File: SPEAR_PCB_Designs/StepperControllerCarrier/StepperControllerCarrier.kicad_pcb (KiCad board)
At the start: 2 copper layers, 108 x 49 mm, 19 parts, among them J1 Conn_01x02_Pin, J2 Conn_01x02_Pin, J3 Conn_01x02_Pin, J4 Conn_01x02_Pin, J5 Conn_01x04_Pin, U1 AP63203WU

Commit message: Fixed this finally
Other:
- board text removed: "2973"
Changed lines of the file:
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@@
 			(drillshape 0)
 			(scaleselection 1)
-			(outputdirectory "Fabrication")
+			(outputdirectory "C:/Users/Ammar/Spear/Stepper_Motor_Controller_Carrier_Board/Fabrication/")
 		)
 	)
@@
 		)
 		(property "Value" "Motor_Driver_Board_2973"
-			(at 12.7 19.82 0)
+			(at 12.7 17.8 0)
 			(unlocked yes)
 			(layer "F.Fab")
@@
 			)
 		)
-		(model "${SPEAR_PCB_2026_DIR}/SPEAR_3D_Models/SPEAR_MotorControllerCarrier/tb67s2x9ftg-stepper-motor-driver-carrier.step"
-			(offset
-				(xyz 0 -35.5 8.5)
-			)
-			(scale
-				(xyz 1 1 1)
-			)
-			(rotate
-				(xyz -0 -0 -0)
-			)
-		)
 	)
 	(footprint "SPEAR_Connectors:JST_XH_S4B-XH-A-1_1x04_P2.50mm_Horizontal"
@@
 		)
 	)
-	(gr_text "2973"
-		(at 167 99 0)
-		(layer "F.SilkS")
-		(effects
-			(font
-				(size 1 1)
-				(thickness 0.15)
-			)
-		)
-	)
 	(gr_text "MOTOR B"
 		(at 184.25 108.5 270)
@@
 	)
 	(segment
-		(start 152.2 112.55)
-		(end 152.2 110.26)
+		(start 152 112.75)
+		(end 152 110.46)
 		(width 0.3)
 		(layer "F.Cu")
@@
 	)
 	(segment
-		(start 138.98 114.1)
-		(end 139.175 114.295)
+		(start 139.175 114.295)
+		(end 150.455 114.295)
 		(width 0.3)
 		(layer "F.Cu")
@@
 	)
 	(segment
-		(start 150.455 114.295)
-		(end 152.2 112.55)
+		(start 152 110.46)
+		(end 154.57 107.89)
 		(width 0.3)
 		(layer "F.Cu")
@@
 	)
 	(segment
-		(start 152.2 110.26)
-		(end 154.57 107.89)
+		(start 150.455 114.295)
+		(end 152 112.75)
 		(width 0.3)
 		(layer "F.Cu")
@@
 	)
 	(segment
-		(start 139.175 114.295)
-		(end 150.455 114.295)
+		(start 138.98 114.1)
+		(end 139.175 114.295)
 		(width 0.3)
 		(layer "F.Cu")

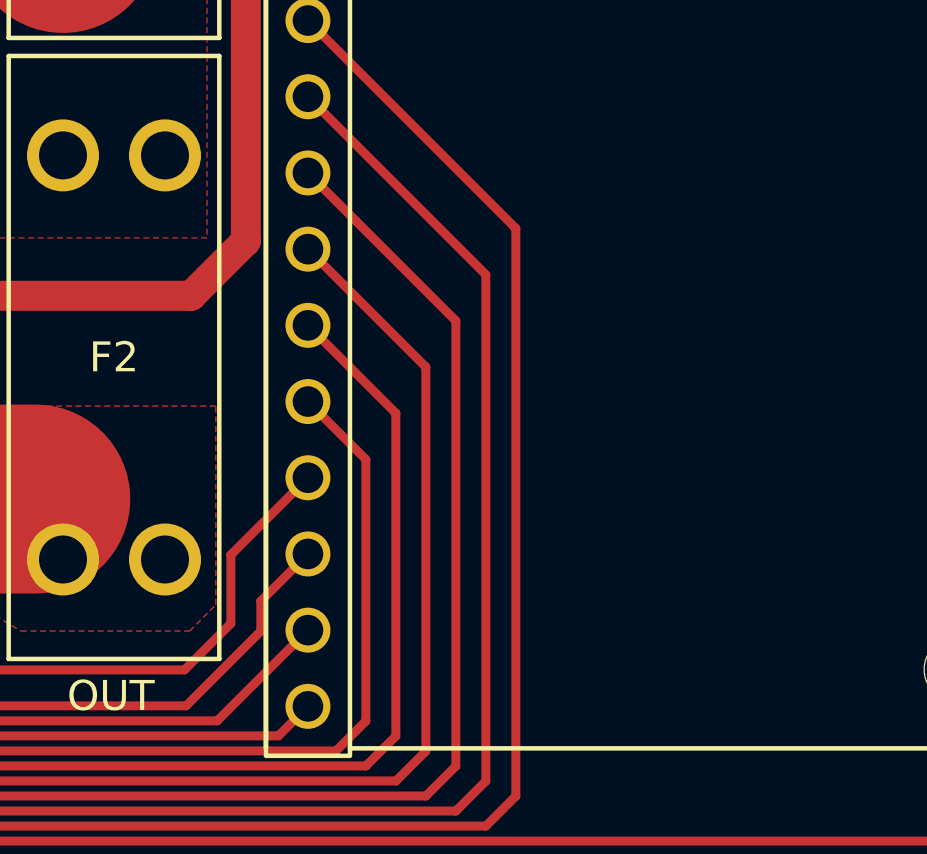
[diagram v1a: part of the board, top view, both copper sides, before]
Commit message: created gerbers for stepper controller board
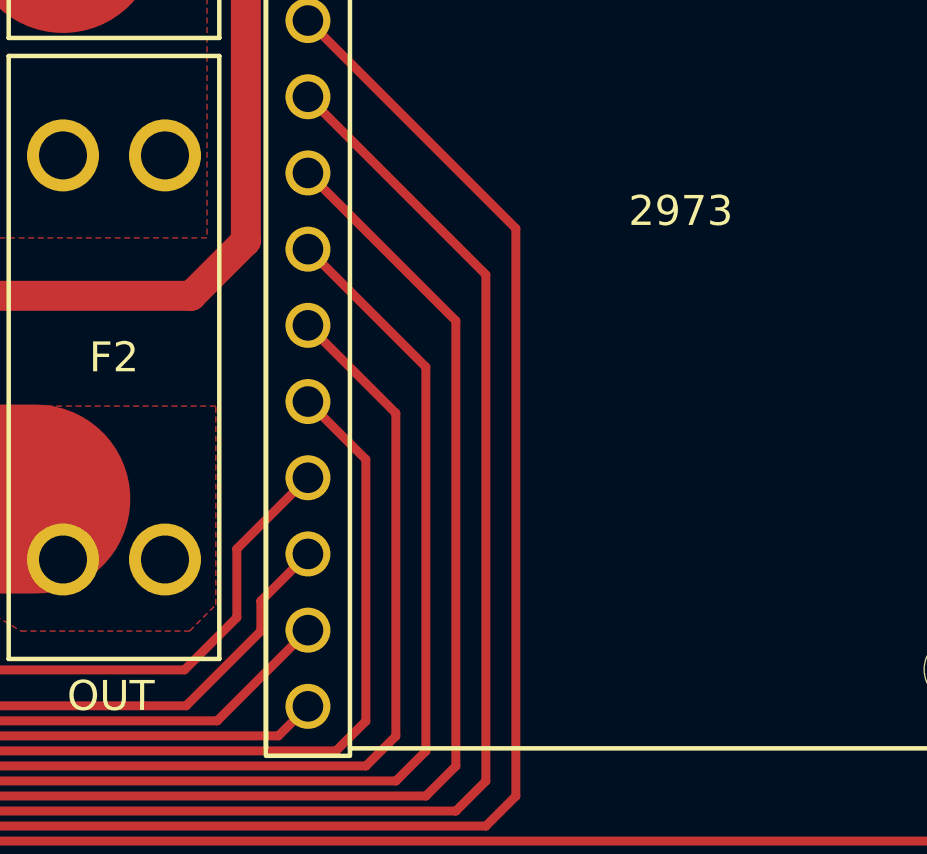
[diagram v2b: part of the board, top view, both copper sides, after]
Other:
- board text added: "2973"
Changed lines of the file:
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@@
 		)
 		(property "Value" "Motor_Driver_Board_2973"
-			(at 12.7 17.8 0)
+			(at 12.7 19.82 0)
 			(unlocked yes)
 			(layer "F.Fab")
@@
 			)
 		)
+		(model "${SPEAR_PCB_2026_DIR}/SPEAR_3D_Models/SPEAR_MotorControllerCarrier/tb67s2x9ftg-stepper-motor-driver-carrier.step"
+			(offset
+				(xyz 0 -35.5 8.5)
+			)
+			(scale
+				(xyz 1 1 1)
+			)
+			(rotate
+				(xyz -0 -0 -0)
+			)
+		)
 	)
 	(footprint "SPEAR_Connectors:JST_XH_S4B-XH-A-1_1x04_P2.50mm_Horizontal"
@@
 		)
 	)
+	(gr_text "2973"
+		(at 167 99 0)
+		(layer "F.SilkS")
+		(effects
+			(font
+				(size 1 1)
+				(thickness 0.15)
+			)
+		)
+	)
 	(gr_text "MOTOR B"
 		(at 184.25 108.5 270)
@@
 	)
 	(segment
-		(start 152 112.75)
-		(end 152 110.46)
+		(start 152.2 112.55)
+		(end 152.2 110.26)
 		(width 0.3)
 		(layer "F.Cu")
@@
 	)
 	(segment
-		(start 139.175 114.295)
-		(end 150.455 114.295)
+		(start 138.98 114.1)
+		(end 139.175 114.295)
 		(width 0.3)
 		(layer "F.Cu")
@@
 	)
 	(segment
-		(start 152 110.46)
-		(end 154.57 107.89)
+		(start 150.455 114.295)
+		(end 152.2 112.55)
 		(width 0.3)
 		(layer "F.Cu")
@@
 	)
 	(segment
-		(start 150.455 114.295)
-		(end 152 112.75)
+		(start 152.2 110.26)
+		(end 154.57 107.89)
 		(width 0.3)
 		(layer "F.Cu")
@@
 	)
 	(segment
-		(start 138.98 114.1)
-		(end 139.175 114.295)
+		(start 139.175 114.295)
+		(end 150.455 114.295)
 		(width 0.3)
 		(layer "F.Cu")
